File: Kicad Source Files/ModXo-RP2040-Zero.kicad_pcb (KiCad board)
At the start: 2 copper layers, 42 x 30 mm, 15 parts, among them J1 XBOX_LPC, U1 RP2040-Zero

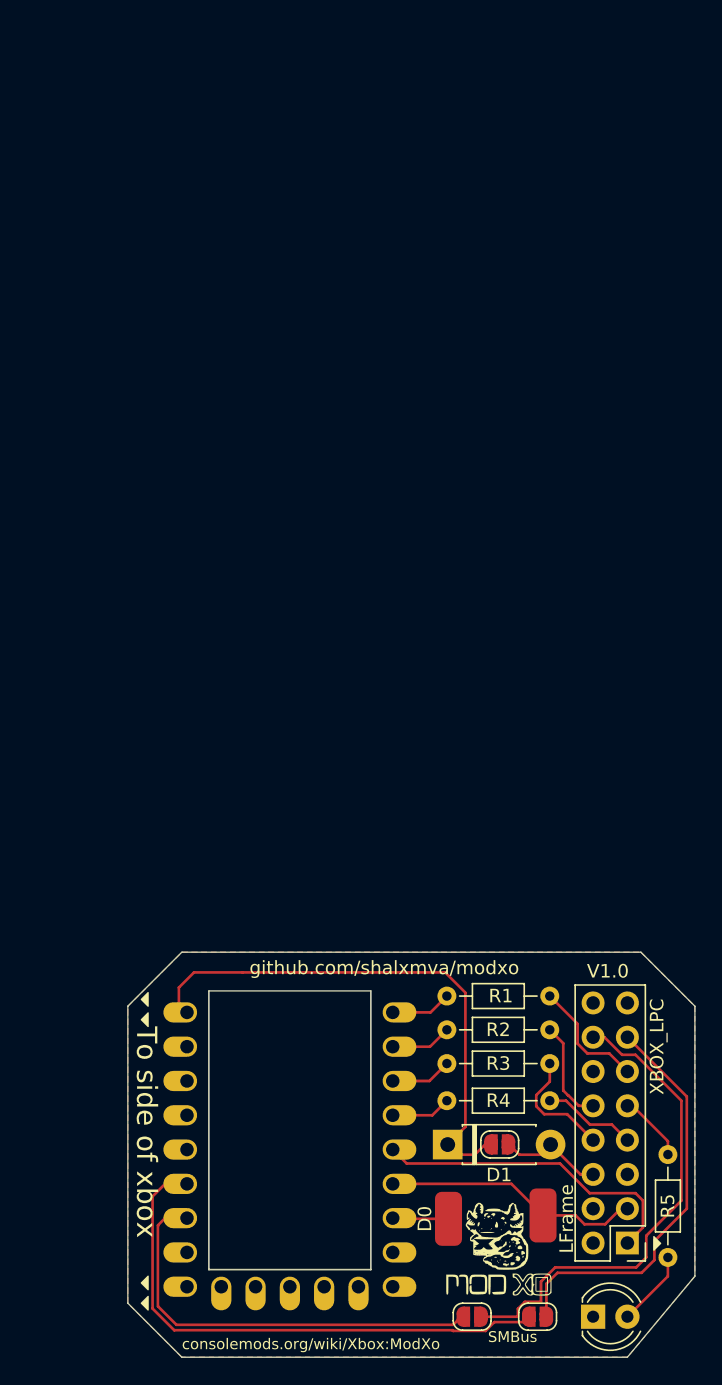
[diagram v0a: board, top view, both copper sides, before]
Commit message: Added images
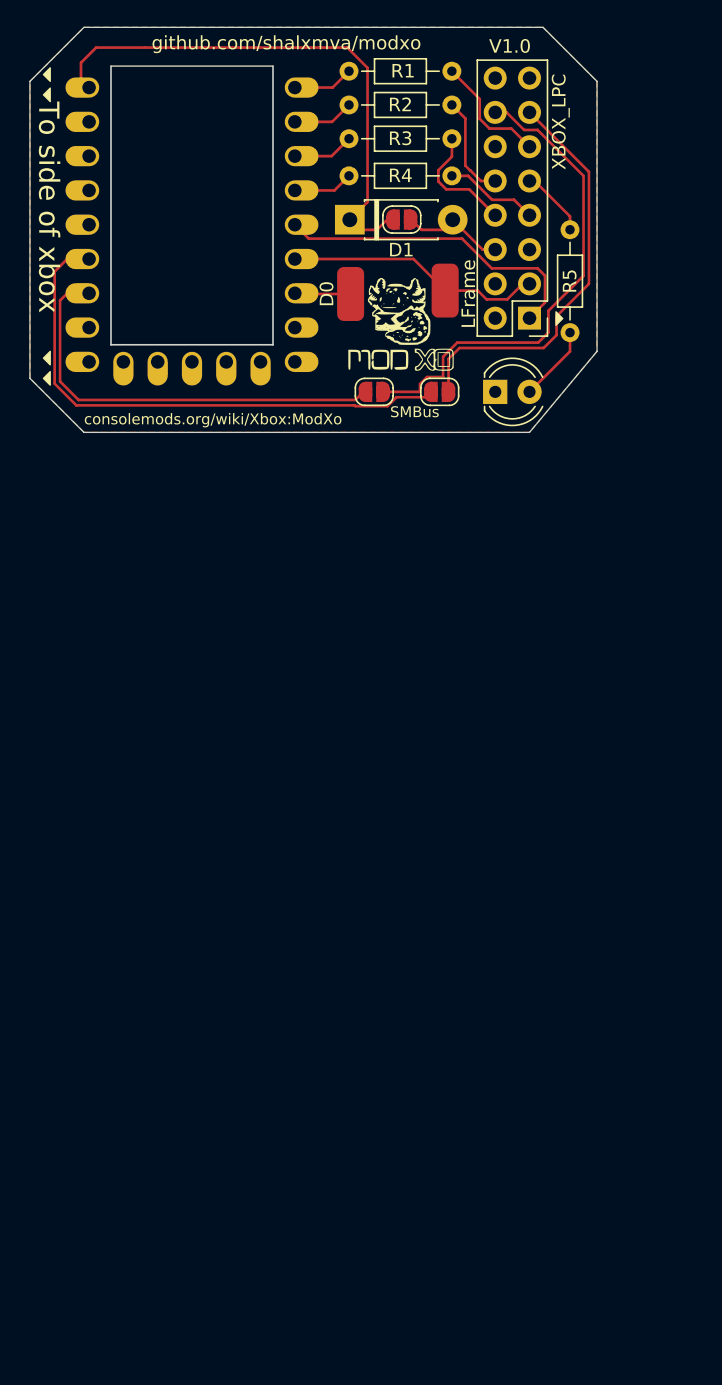
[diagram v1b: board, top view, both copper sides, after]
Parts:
- moved R5 68.9 mm to (118.8, 65.5)
- moved D0 68.9 mm to (102.5, 70.2)
- moved D1 68.9 mm to (102.4, 64.8)
- moved D2 68.9 mm to (113.2, 77.5)
- moved G*** 68.9 mm to (106.2, 72.5)
- moved J1 68.9 mm to (115.7, 72.1)
- moved JP1 68.9 mm to (104.2, 77.5)
- moved JP2 68.9 mm to (109.1, 77.5)
- moved LFrame1 68.9 mm to (109.5, 70.0)
- moved R1 68.9 mm to (102.4, 53.8)
- moved R2 68.9 mm to (102.4, 56.2)
- moved R3 68.9 mm to (102.4, 58.8)
- moved R4 68.9 mm to (102.4, 61.5)
- moved U1 68.9 mm to (90.8, 65.1)
- moved JP3 68.9 mm to (106.3, 64.7)
